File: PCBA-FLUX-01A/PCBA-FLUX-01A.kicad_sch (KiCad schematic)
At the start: 0 parts

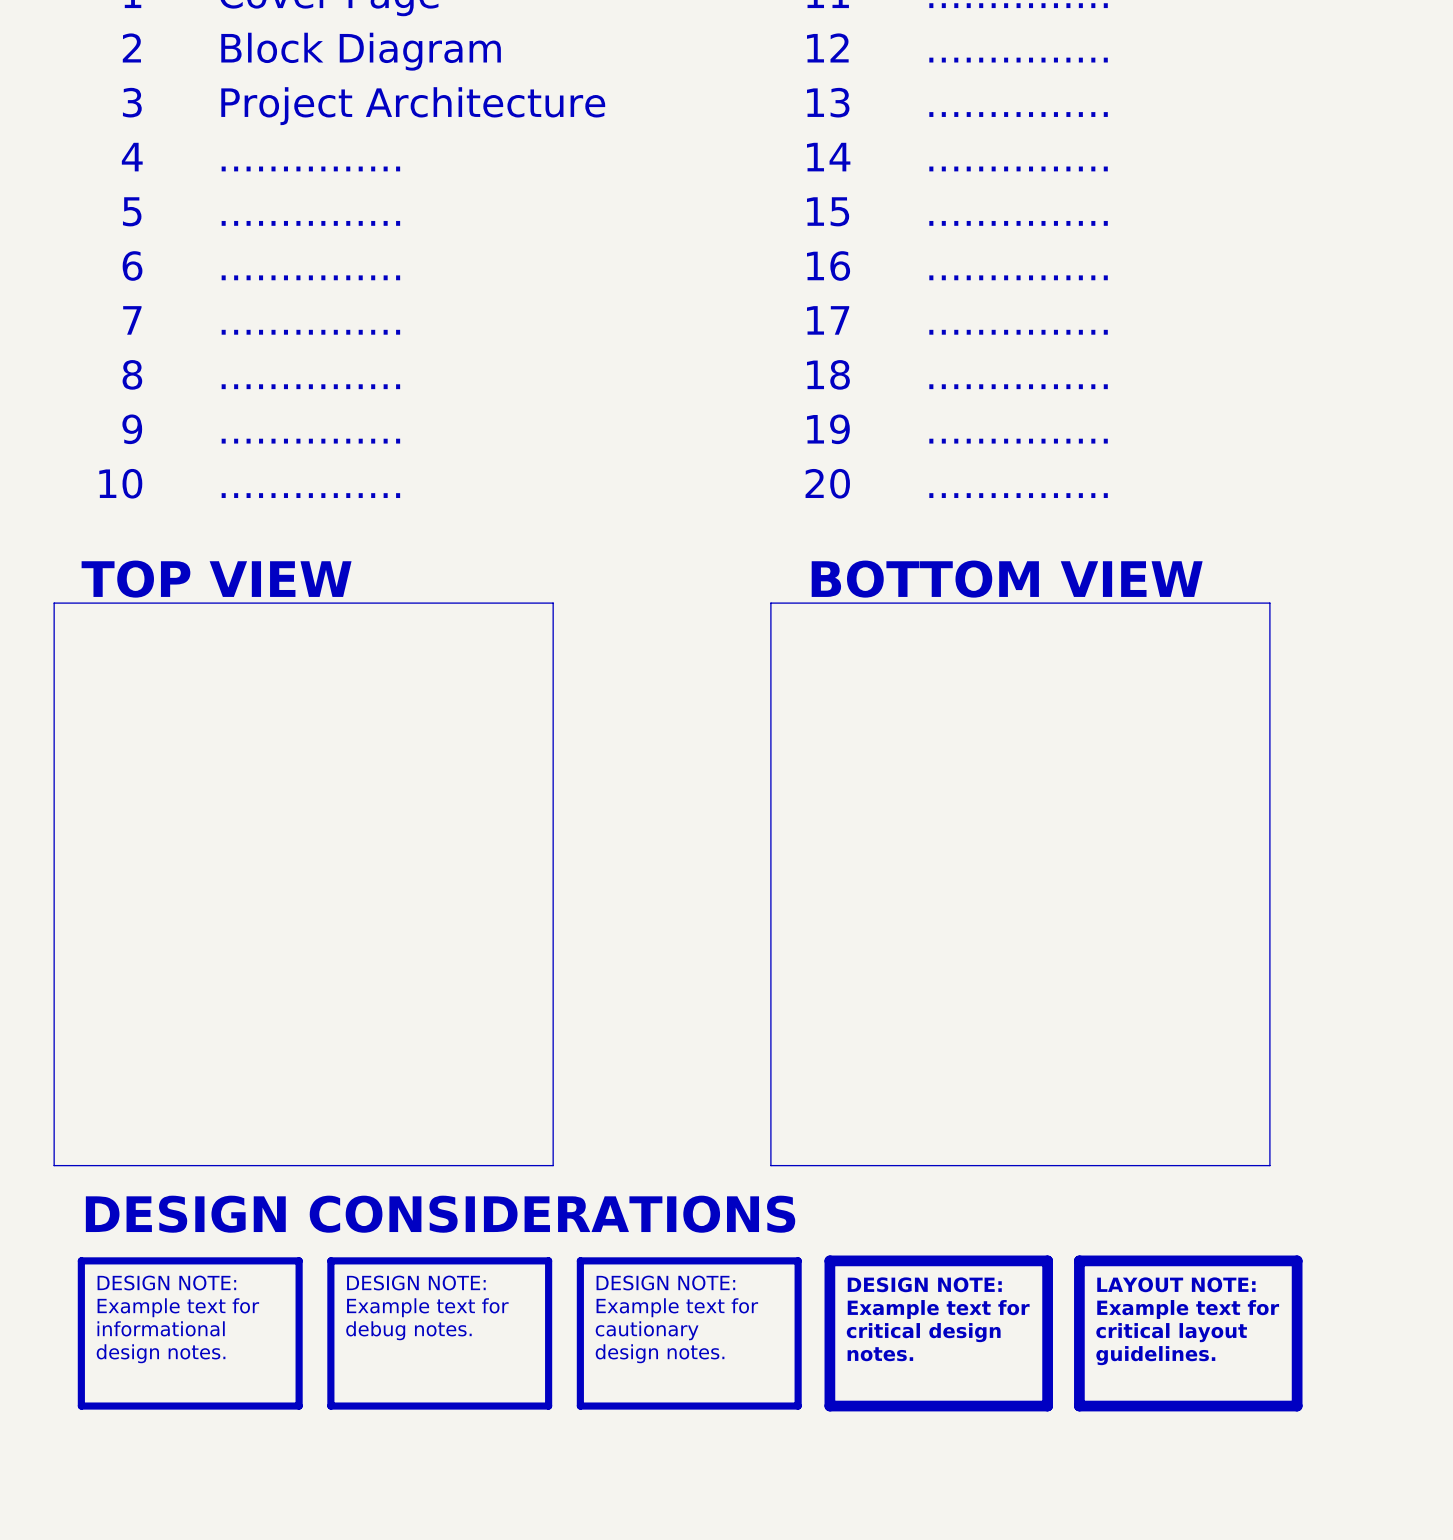
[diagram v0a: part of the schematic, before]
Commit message: Finished inverter design and started working on MCU pin out
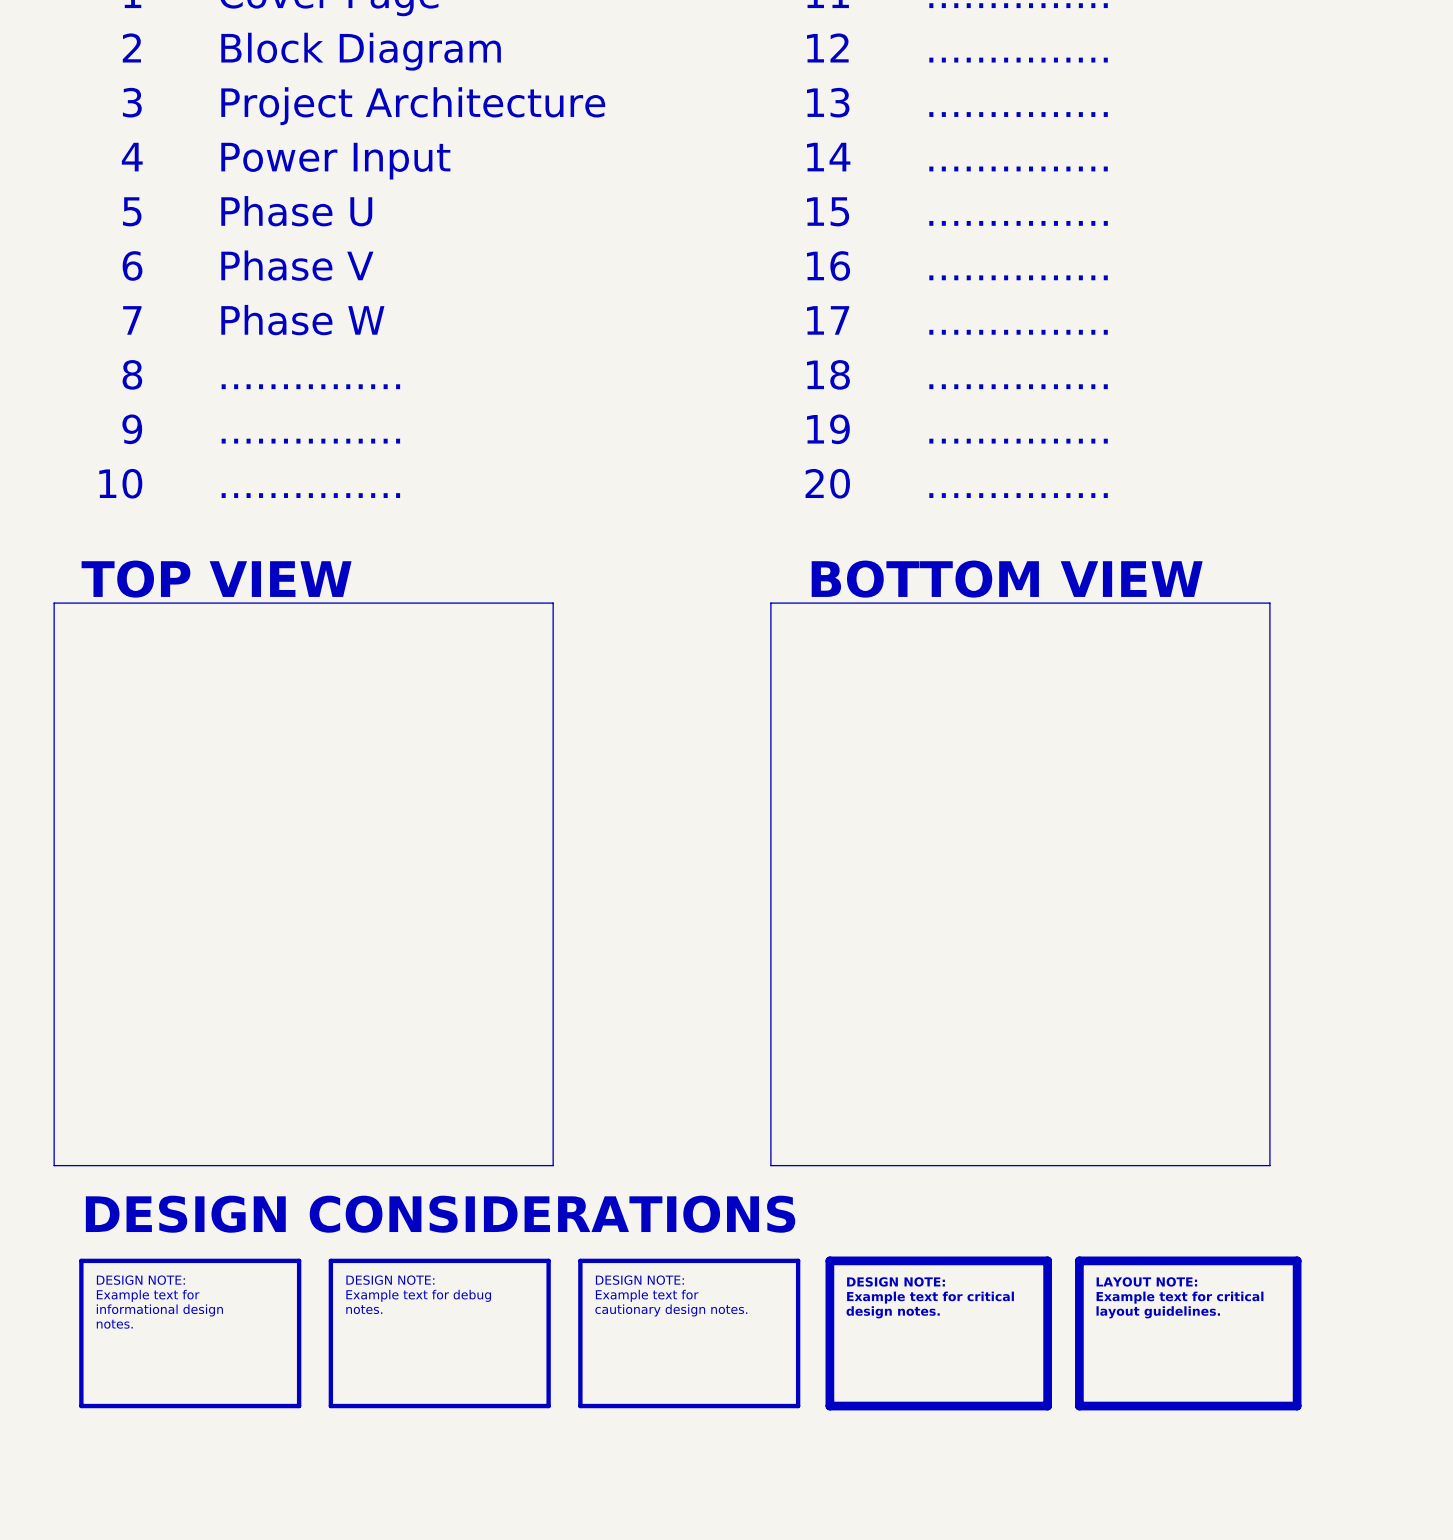
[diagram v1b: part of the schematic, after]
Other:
- note added: "Phase U"
- note added: "Phase V"
- note added: "Phase W"
- note added: "Power Input"
- company: (none) -> Jovanovski Laboratory - JLAB
